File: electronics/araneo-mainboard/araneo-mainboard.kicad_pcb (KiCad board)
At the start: 2 copper layers, 71.5 x 68.5 mm, 60 parts, among them J2 OLED, J3 GPIO, SW1 SW, SW2 SW, U1 IMU, U2 L78M05CDT, U3 BD9C601EFJ, U4 POWER, U5 PAM8403D

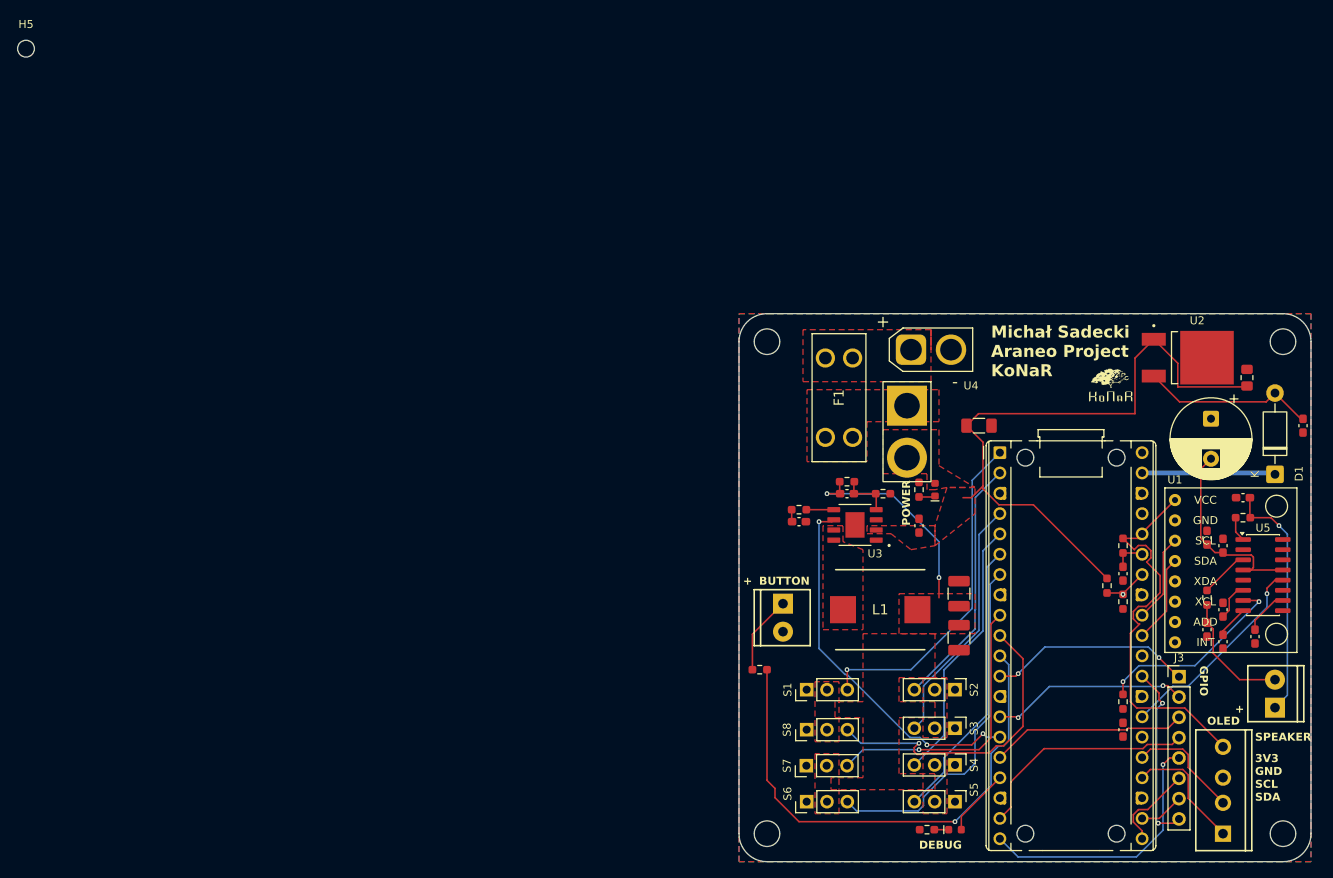
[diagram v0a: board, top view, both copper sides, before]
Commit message: electronics: add capacitor filters and Schottky diode
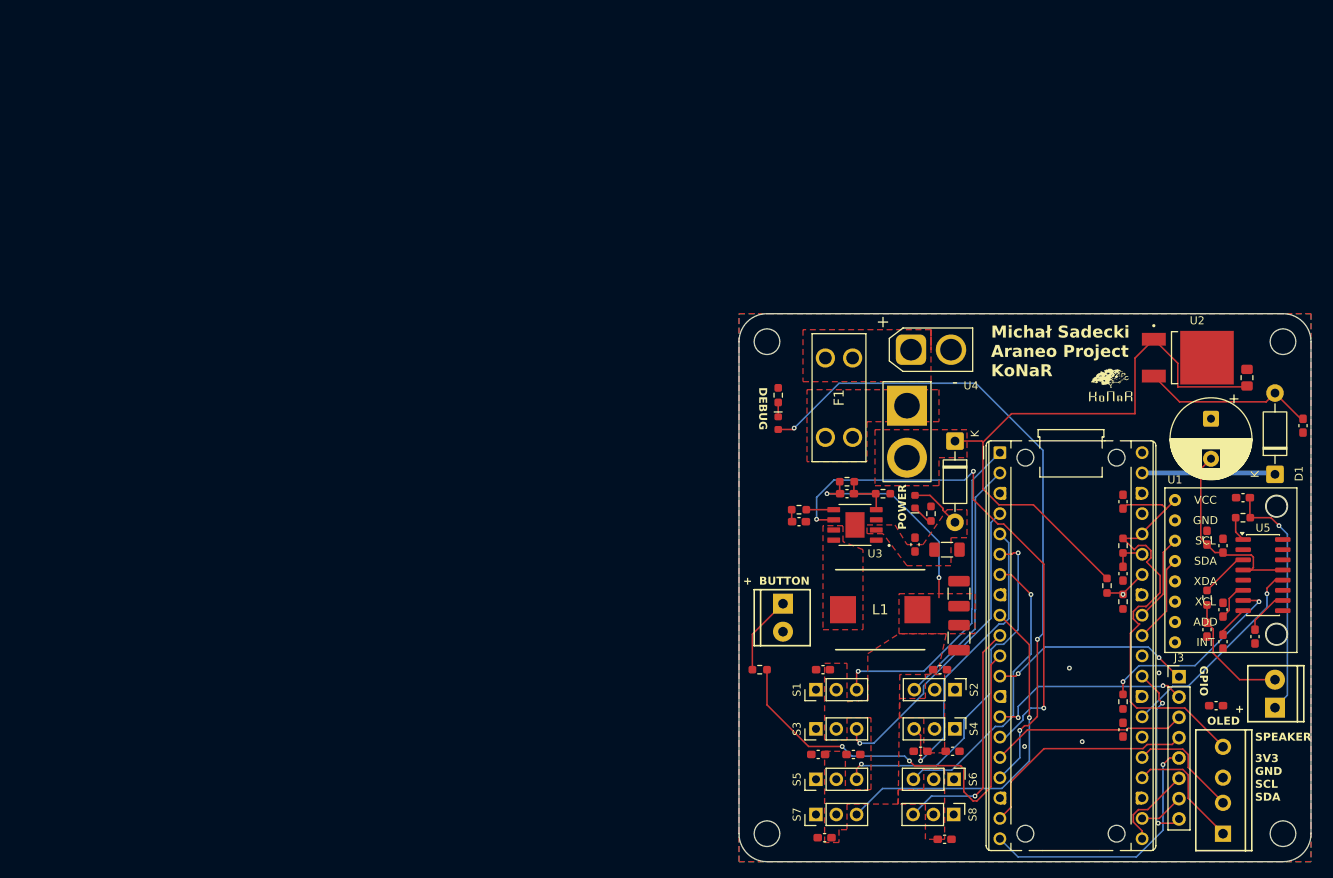
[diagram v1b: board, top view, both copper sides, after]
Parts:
- removed H5: MountingHole, MountingHole:MountingHole_2.1mm
- added C19: 0.1uF, Capacitor_SMD:C_0603_1608Metric_Pad1.08x0.95mm_HandSolder, F.Cu at (151.1, 84.5)
- added C20: 0.1uF, Capacitor_SMD:C_0603_1608Metric_Pad1.08x0.95mm_HandSolder, F.Cu at (139.5, 59.0)
- added C21: 0.1uF, Capacitor_SMD:C_0603_1608Metric_Pad1.08x0.95mm_HandSolder, F.Cu at (102.2, 101.0)
- added C22: 0.1uF, Capacitor_SMD:C_0603_1608Metric_Pad1.08x0.95mm_HandSolder, F.Cu at (101.4, 90.6)
- added C23: 0.1uF, Capacitor_SMD:C_0603_1608Metric_Pad1.08x0.95mm_HandSolder, F.Cu at (105.8, 90.6)
- added C24: 0.1uF, Capacitor_SMD:C_0603_1608Metric_Pad1.08x0.95mm_HandSolder, F.Cu at (117.2, 101.2)
- added C25: 0.1uF, Capacitor_SMD:C_0603_1608Metric_Pad1.08x0.95mm_HandSolder, F.Cu at (118.2, 90.2)
- added C26: 0.1uF, Capacitor_SMD:C_0603_1608Metric_Pad1.08x0.95mm_HandSolder, F.Cu at (114.2, 90.2)
- added C27: 0.1uF, Capacitor_SMD:C_0603_1608Metric_Pad1.08x0.95mm_HandSolder, F.Cu at (102.0, 80.0)
- added C28: 0.1uF, Capacitor_SMD:C_0603_1608Metric_Pad1.08x0.95mm_HandSolder, F.Cu at (116.6, 80.0)
- added D4: D_Schottky, Diode_THT:D_DO-41_SOD81_P10.16mm_Horizontal, F.Cu at (118.5, 51.4)
- C1, C10: value 100nF -> 0.1uF
- C13, C14: value 470nF -> 0.47uF
- C2: value 330nF -> 0.33uF
- R13: value 1k -> 1.2k
- moved R13 57.4 mm to (96.4, 45.7), turned to 90 degrees
- moved D3 55.4 mm to (96.4, 49.2), turned to -90 degrees
- moved S8 21.2 mm to (118.3, 98.1), turned to -90 degrees
- moved S6 18.6 mm to (118.4, 93.7), turned to -90 degrees
- moved S5 17.6 mm to (101.1, 93.7), turned to 90 degrees
- moved S3 17.4 mm to (101.1, 87.4), turned to 90 degrees
- moved C3 16.0 mm to (117.5, 65.0)
- moved S7 6.22 mm to (101.1, 98.1)
- moved S4 4.51 mm to (118.5, 87.4)
- moved R7 3.35 mm to (115.5, 60.5)
- moved D2 2.92 mm to (113.5, 59.0)
- moved C4 2.41 mm to (113.5, 64.4)
- moved S1 1.16 mm to (101.1, 82.5)
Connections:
- C3 pad 2: /+7.4V_F -> Net-(D2-A)
- C4 pad 2: /+7.4V_F -> Net-(D2-A)
- D2 pad 2: /+7.4V_F -> Net-(D2-A)
- U3 pad 2: /+7.4V_F -> Net-(D2-A)
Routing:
- net /D1: track 8.49 -> 82.4 mm, vias 0 -> 3
- net /EN: track 46.2 -> 67.2 mm, vias 3 -> 4
- net /PWM5: track 35.4 -> 45.3 mm, vias 0 -> 2
- net /PWM7: track 35.2 -> 44.1 mm
- net /PWM8: track 38.7 -> 30.1 mm
- net /BUTTON: track 64.5 -> 56.6 mm, vias 1 -> 2
- net /PWM3: track 31.3 -> 39.0 mm, vias 0 -> 1
- net /PWM6: track 44.4 -> 36.8 mm, vias 0 -> 1
- net Net-(D2-A): track 0.00 -> 6.54 mm
- net /+3V3: track 49.7 -> 55.5 mm
- net /PWM4: track 33.3 -> 38.1 mm, vias 0 -> 1
- net /+7.4V_F: track 80.5 -> 76.2 mm
- net /GPIO10: track 24.7 -> 25.5 mm
- net Net-(D2-K): track 2.05 -> 2.67 mm
- net GND: vias 0 -> 4
- added copper zone on F.Cu, net Net-(D2-A)

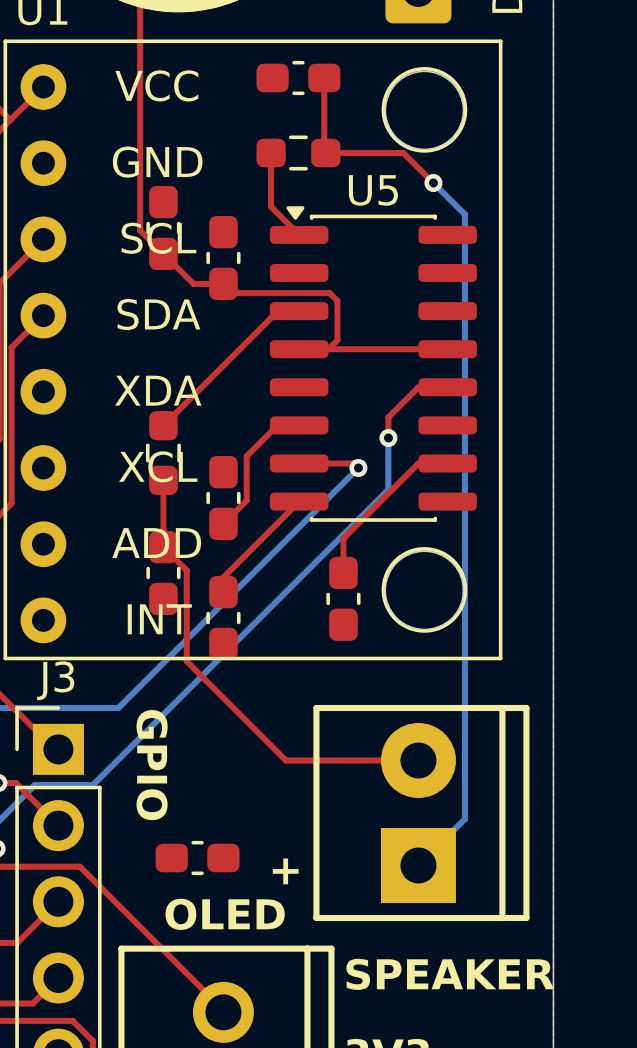
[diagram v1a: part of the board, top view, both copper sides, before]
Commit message: electronics: new buck, regulator and improve schematic
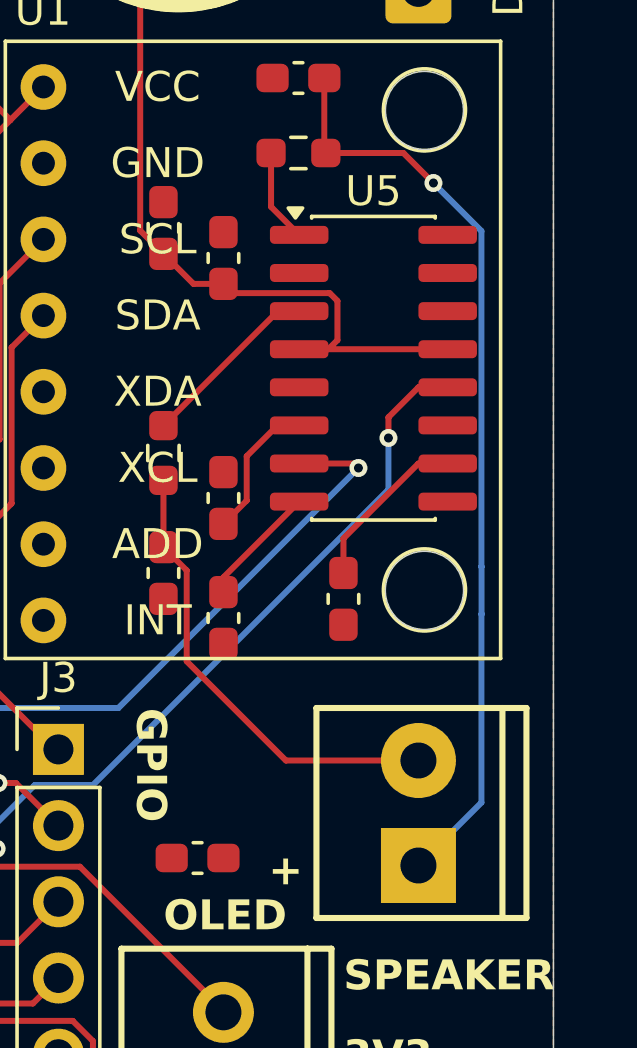
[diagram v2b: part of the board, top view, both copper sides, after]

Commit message: electronics: pcb v3
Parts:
- removed C3: 10uF, Capacitor_SMD:C_1206_3216Metric_Pad1.33x1.80mm_HandSolder
- removed C4: 0.1uF, Capacitor_SMD:C_0603_1608Metric_Pad1.08x0.95mm_HandSolder
- removed C5: OPEN, Capacitor_SMD:C_0603_1608Metric_Pad1.08x0.95mm_HandSolder
- removed C6, C7: 22uF, Capacitor_SMD:C_1210_3225Metric_Pad1.33x2.70mm_HandSolder
- removed C8: 1.5nF, Capacitor_SMD:C_0603_1608Metric_Pad1.08x0.95mm_HandSolder
- removed D4: D_Schottky, Diode_THT:D_DO-41_SOD81_P10.16mm_Horizontal
- removed F1: Fuse, custom_footprints:3568
- removed R1: 1.2k, Resistor_SMD:R_0603_1608Metric_Pad0.98x0.95mm_HandSolder
- removed R2: 7.87k, Resistor_SMD:R_0603_1608Metric_Pad0.98x0.95mm_HandSolder
- removed R3: 39k, Resistor_SMD:R_0603_1608Metric_Pad0.98x0.95mm_HandSolder
- removed R7: 4.7k, Resistor_SMD:R_0603_1608Metric_Pad0.98x0.95mm_HandSolder
- removed R8: 100, Resistor_SMD:R_0603_1608Metric_Pad0.98x0.95mm_HandSolder
- removed SW1: SW, PCM_SparkFun-Connector:ScrewTerminal_1x02_P5.0mm
- removed U2: L78M05CDT, custom_footprints:VREG_L78M05CDT
- added C29: 1uF, Capacitor_SMD:C_0603_1608Metric_Pad1.08x0.95mm_HandSolder, F.Cu at (154.0, 38.6)
- added C30: 100nF, Capacitor_SMD:C_0603_1608Metric_Pad1.08x0.95mm_HandSolder, F.Cu at (147.6, 37.4)
- added C31: 10uF, Capacitor_SMD:C_1206_3216Metric_Pad1.33x1.80mm_HandSolder, F.Cu at (104.4, 57.2)
- added C32: 10uF, Capacitor_SMD:C_1206_3216Metric_Pad1.33x1.80mm_HandSolder, F.Cu at (104.4, 60.2)
- added C33: 0.1uF, Capacitor_SMD:C_0603_1608Metric_Pad1.08x0.95mm_HandSolder, F.Cu at (105.2, 62.6)
- added C34: 22uF, Capacitor_SMD:C_1210_3225Metric_Pad1.33x2.70mm_HandSolder, F.Cu at (117.2, 67.0)
- added C36: 22uF, Capacitor_SMD:C_1210_3225Metric_Pad1.33x2.70mm_HandSolder, F.Cu at (117.2, 74.8)
- added C37: 22uF, Capacitor_SMD:C_1210_3225Metric_Pad1.33x2.70mm_HandSolder, F.Cu at (117.2, 78.8)
- added C38: 22uF, Capacitor_SMD:C_1210_3225Metric_Pad1.33x2.70mm_HandSolder, F.Cu at (117.2, 71.0)
- added CFF1: 100nF, Capacitor_SMD:C_0603_1608Metric_Pad1.08x0.95mm_HandSolder, F.Cu at (117.0, 62.8)
- added D5: POWER_LED, PCM_SparkFun-LED:LED_0603_1608Metric, F.Cu at (105.4, 55.0)
- added D6: D_Schottky, Diode_THT:D_DO-41_SOD81_P10.16mm_Horizontal, F.Cu at (110.5, 39.4)
- added F2: Fuse, custom_footprints:3568, F.Cu at (117.7, 56.8)
- added FB3: FerriteBead, Resistor_SMD:R_0603_1608Metric_Pad0.98x0.95mm_HandSolder, F.Cu at (137.8, 63.1)
- added J1: GPIO2, Connector_PinHeader_2.54mm:PinHeader_1x06_P2.54mm_Vertical, F.Cu at (119.4, 89.2)
- added PS1: TPS566242DRLR, custom_footprints:SOT50P160X60-6N, F.Cu at (110.8, 62.8)
- added R12: 43k, Resistor_SMD:R_0603_1608Metric_Pad0.98x0.95mm_HandSolder, F.Cu at (114.2, 63.8)
- added R15: 1k, Resistor_SMD:R_0603_1608Metric_Pad0.98x0.95mm_HandSolder, F.Cu at (105.2, 53.2)
- added R4: 120, Resistor_SMD:R_0603_1608Metric_Pad0.98x0.95mm_HandSolder, F.Cu at (150.4, 38.6)
- added R5: 360, Resistor_SMD:R_0603_1608Metric_Pad0.98x0.95mm_HandSolder, F.Cu at (154.0, 36.6)
- added R6: 4.7k, Resistor_SMD:R_0603_1608Metric_Pad0.98x0.95mm_HandSolder, F.Cu at (114.2, 62.0)
- added SW3: SW, PCM_SparkFun-Connector:ScrewTerminal_1x02_P5.0mm, F.Cu at (101.0, 45.2)
- C1: value 0.1uF -> 22uF; footprint Capacitor_SMD:C_0603_1608Metric_Pad1.08x0.95mm_HandSolder -> Capacitor_Tantalum_SMD:CP_EIA-3528-15_AVX-H_HandSolder
- C2: value 0.33uF -> 22uF; footprint Capacitor_SMD:C_0805_2012Metric_Pad1.18x1.45mm_HandSolder -> Capacitor_SMD:C_1210_3225Metric_Pad1.33x2.70mm_HandSolder
- D1: value D_Schottky -> D
- D2: value BUCK_LED -> SMF9V0A; footprint PCM_SparkFun-LED:LED_0603_1608Metric -> Diode_SMD:D_SMF
- J3: value GPIO -> GPIO1; footprint Connector_PinHeader_2.54mm:PinHeader_1x08_P2.54mm_Vertical -> Connector_PinHeader_2.54mm:PinHeader_1x02_P2.54mm_Vertical
- U3: value BD9C601EFJ -> TLV1117-ADJ; footprint custom_footprints:SOIC127P600X100-9N -> Package_TO_SOT_SMD:SOT-223-3_TabPin2
- moved D3 51.3 mm to (147.6, 52.2)
- moved R13 49.7 mm to (145.6, 52.4), turned to -90 degrees
- moved U3 47.2 mm to (149.8, 44.2), turned to -90 degrees
- moved C17 36.2 mm to (149.8, 84.8), turned to 90 degrees
- moved R14 31.9 mm to (105.4, 50.2)
- moved D1 22.4 mm to (143.8, 38.7), turned to -90 degrees
- moved SW2 18.9 mm to (97.3, 52.9)
- moved C2 14.6 mm to (140.4, 44.2), turned to -90 degrees
- moved C19 14.1 mm to (147.2, 98.0), turned to -90 degrees
- moved J3 12.7 mm to (146.4, 93.6), turned to 180 degrees
- moved C26 12.5 mm to (101.8, 91.4)
- moved C23 8.98 mm to (114.4, 93.2)
- moved C20 8.51 mm to (147.8, 57.1)
- moved C1 7.51 mm to (154.6, 50.8), turned to 0 degrees
- moved C28 5.92 mm to (114.2, 85.4)
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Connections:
- net /+3V3_RC renamed +3V3_RC
- net /+6V renamed +6V
- A1 pad 1: /PWM1 -> /EN
- A1 pad 10: /PWM8 -> /PWM6
- A1 pad 11: /BUTTON -> /PWM7
- A1 pad 12: /GPIO9 -> /PWM8
- A1 pad 15: /EN -> /GPIO11
- A1 pad 17: /D1 -> /GPIO13
- A1 pad 2: /PWM2 -> /BUTTON
- A1 pad 21: /GPIO16 -> /SDA_OLED
- A1 pad 22: /GPIO17 -> /SCL_OLED
- A1 pad 24: /SDA_OLED -> /GPIO18
- A1 pad 25: /SCL_OLED -> /GPIO19
- A1 pad 26: /SPEAKER -> /SHDN
- A1 pad 27: /SHDN -> /SPEAKER
- A1 pad 29: /GPIO22 -> /D1
- A1 pad 36: /+3V3 -> +3V3
- A1 pad 39: /+5V_LDO -> +5V
- A1 pad 4: /PWM3 -> /PWM1
- A1 pad 5: /PWM4 -> /PWM2
- A1 pad 6: /PWM5 -> /PWM3
- A1 pad 7: /PWM6 -> /PWM4
- A1 pad 9: /PWM7 -> /PWM5
- C1 pad 1: Net-(D1-A) -> +5V
- C15 pad 1: Net-(U5-VDD) -> +3V3
- C16 pad 2: Net-(C16-Pad2) -> +3V3
- C17 pad 2: Net-(C16-Pad2) -> +3V3
- C18 pad 2: Net-(C16-Pad2) -> +3V3
- C19 pad 1: /+3V3 -> +3V3
- C2 pad 1: /+7.4V_F -> +7.4V_F
- C20 pad 1: /+3V3 -> +3V3
- D1 pad 1: /+5V_LDO -> +7.4V_F
- D1 pad 2: Net-(D1-A) -> +5V
- D2 pad 1: Net-(D2-K) -> +7.4V_F
- D2 pad 2: Net-(D2-A) -> Net-(D2-A2)
- J2 pad 4: /+3V3 -> +3V3
- J3 pad 1: /GPIO9 -> /GPIO18
- J3 pad 2: /GPIO10 -> /GPIO19
- L1 pad 1: Net-(L1-Pad1) -> Net-(PS1-SW)
- R11 pad 1: /+7.4V_F -> +7.4V_F
- U1 pad 1: /+3V3 -> +3V3
- U3 pad 1: GND -> Net-(U3-ADJ)
- U3 pad 2: Net-(D2-A) -> +5V
- U3 pad 3: GND -> +7.4V_F
- U5 pad 13: Net-(C16-Pad2) -> +3V3
- U5 pad 4: Net-(C16-Pad2) -> +3V3
- U5 pad 6: Net-(U5-VDD) -> +3V3
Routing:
- net /+7.4V_F: track 76.2 -> 0.00 mm
- net +7.4V_F: track 0.00 -> 75.3 mm, vias 0 -> 1
- net +3V3: track 0.00 -> 71.5 mm, vias 0 -> 1
- net /+3V3: track 55.5 -> 0.00 mm
- net /D1: track 82.4 -> 32.9 mm, vias 3 -> 2
- net /EN: track 67.2 -> 22.5 mm, vias 4 -> 1
- net /BUTTON: track 56.6 -> 20.0 mm, vias 2 -> 1
- net /GPIO15: track 33.3 -> 5.03 mm, vias 1 -> 0
- net +5V: track 0.00 -> 27.6 mm
- net Net-(C16-Pad2): track 25.7 -> 0.00 mm
- net /GPIO9: track 25.4 -> 0.00 mm, vias 2 -> 0
- net /GPIO14: track 28.4 -> 5.03 mm
- net /GPIO22: track 22.6 -> 0.00 mm, vias 2 -> 0
- net Net-(D1-A): track 21.8 -> 0.00 mm
- net /GPIO10: track 25.5 -> 6.08 mm, vias 2 -> 0
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- added copper zone on F.Cu, net +7.4V_F
- added copper zone on F.Cu, net Net-(D2-A2)
- added copper zone on F.Cu, net Net-(D6-A)
- added copper zone on F.Cu, net Net-(PS1-SW)
- added copper zone on F.Cu, net Net-(SW3-B)
- removed copper zone on F.Cu, net +7.4V
- removed copper zone on F.Cu, net /+7.4V_F
- removed copper zone on F.Cu, net Net-(D2-A)
- removed copper zone on F.Cu, net Net-(L1-Pad1)
- removed copper zone on F.Cu, net Net-(SW1-A)
